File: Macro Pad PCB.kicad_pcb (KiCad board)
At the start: 2 copper layers, 77.8 x 173 mm, 169 parts, among them J1 Debug, Q1 DMG1012T, SW1 PEC11R-4015F-S0024, SW2 PEC11R-4015F-S0024, U1 RP2040, U2 W25Q16JVSNIQ, U3 MIC5365-3.3YC5-TR, U4 IP4234CZ6, Y2 12 MHz

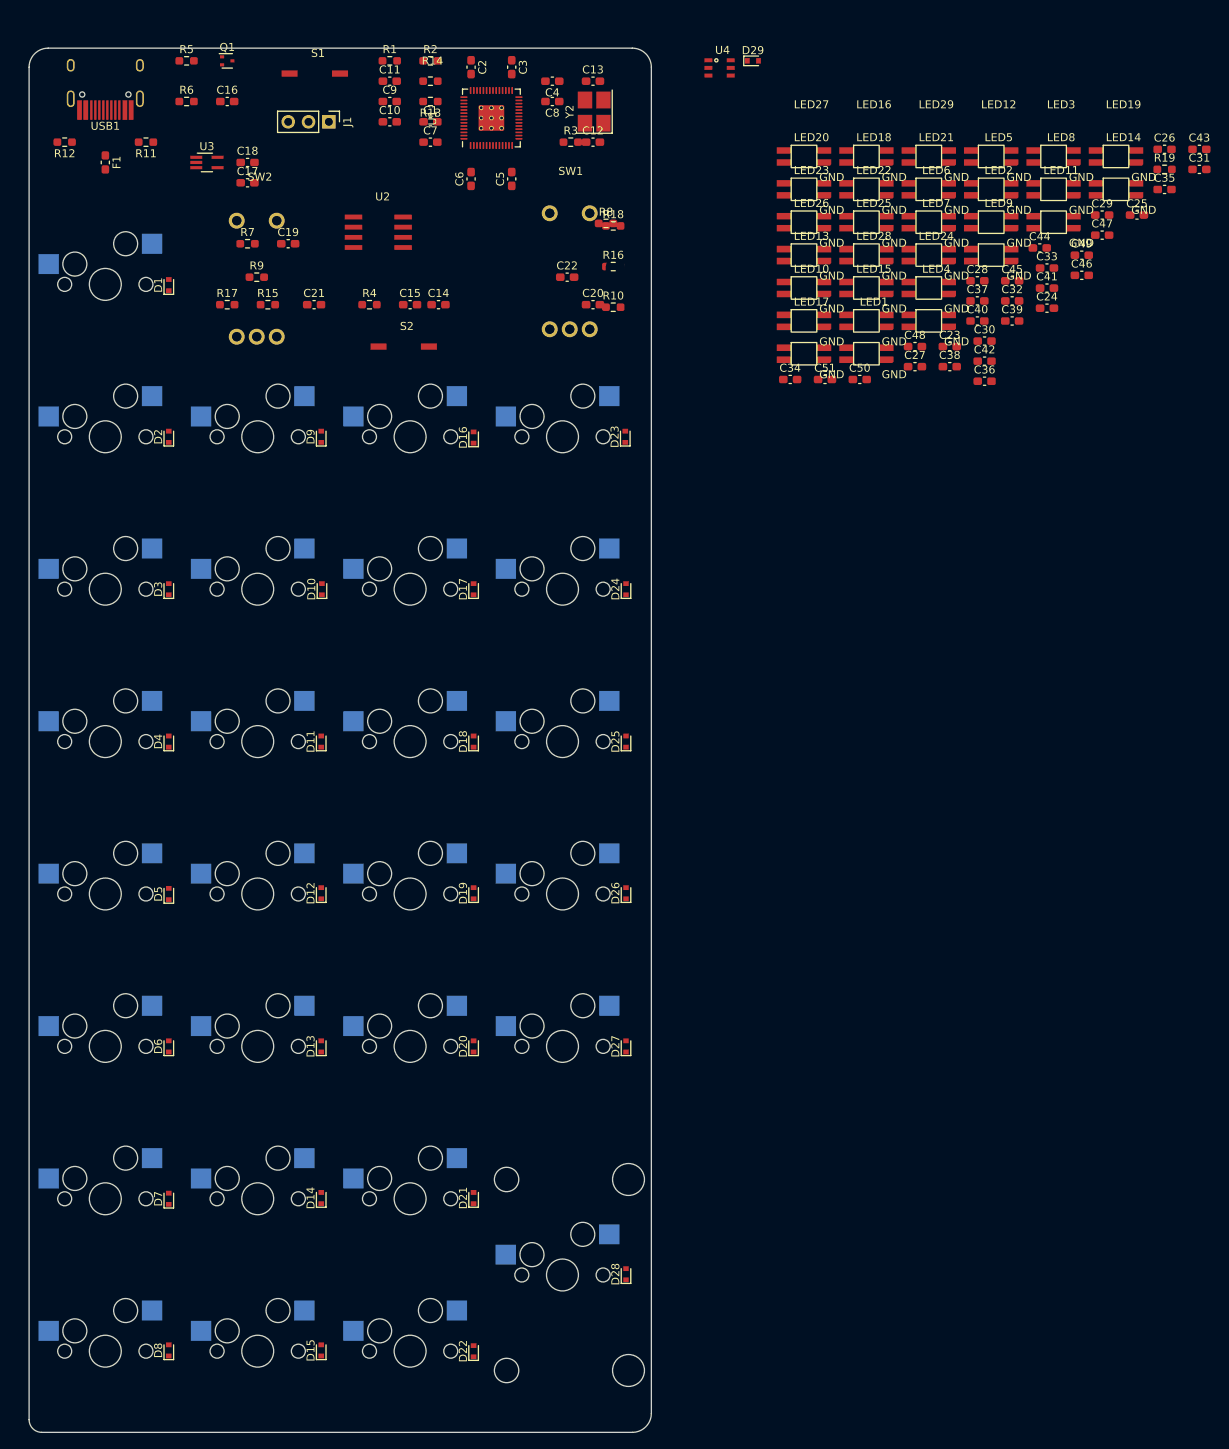
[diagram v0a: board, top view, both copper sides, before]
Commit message: Layout Roughed in, routing started
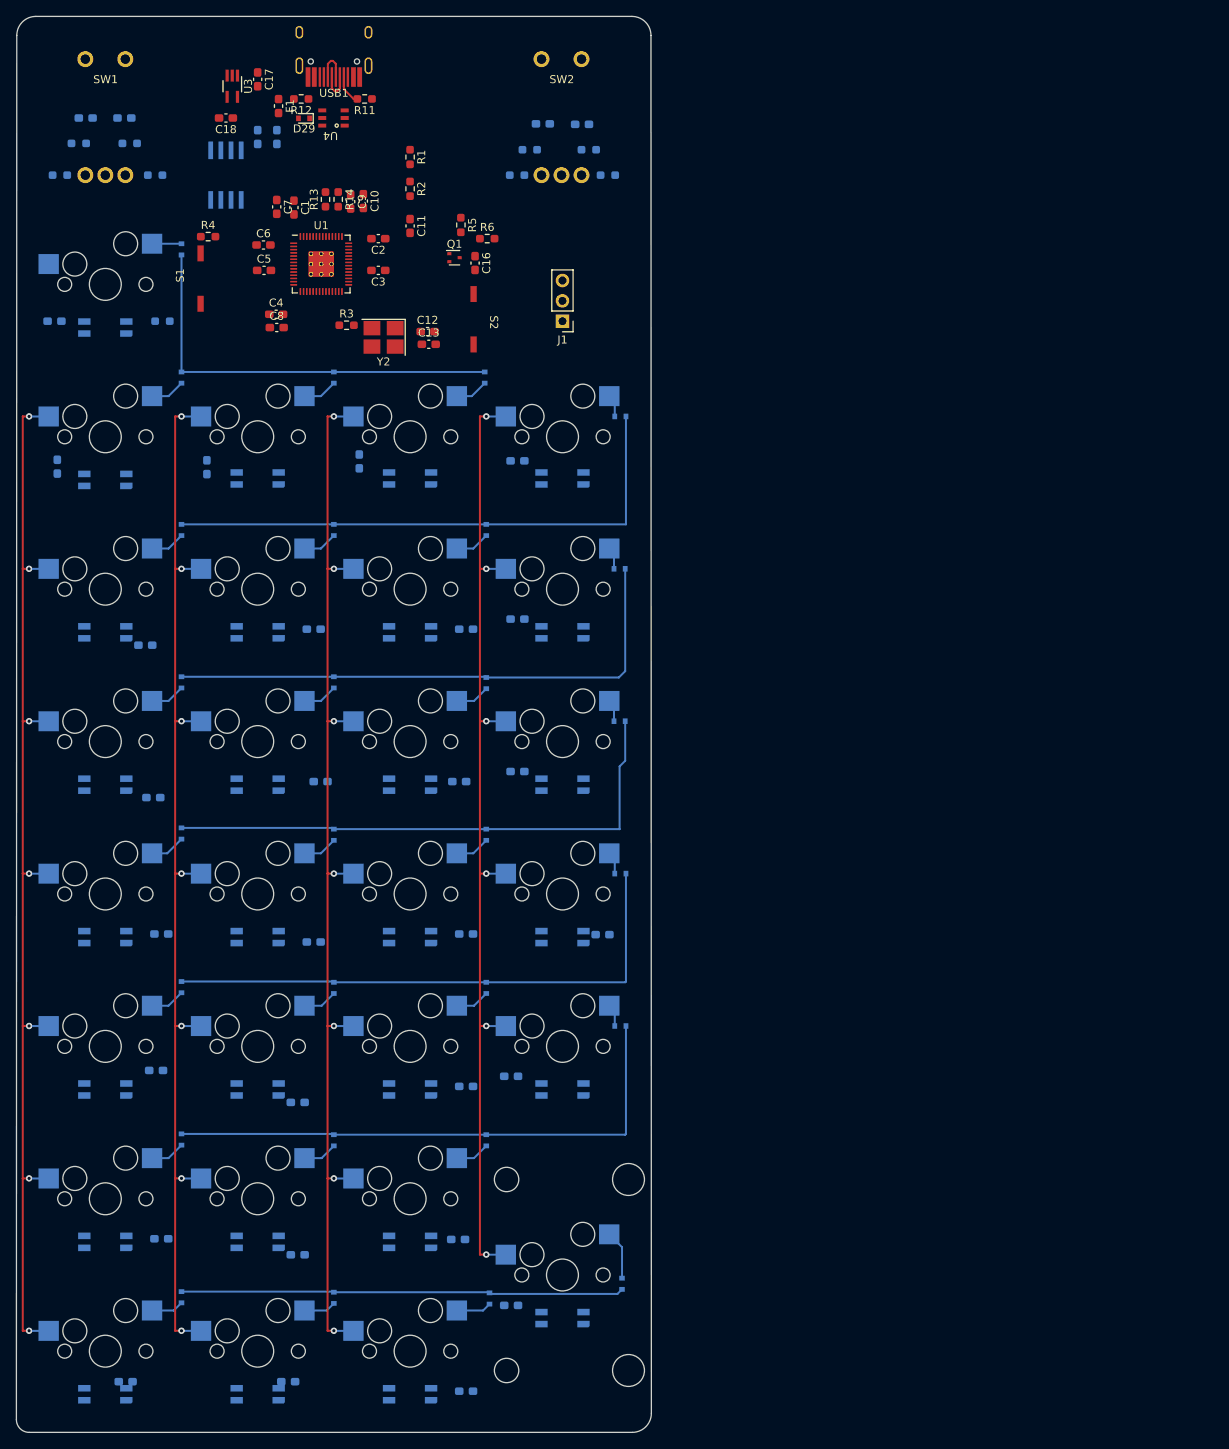
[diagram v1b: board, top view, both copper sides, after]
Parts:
- removed C51: 100nF, Capacitor_SMD:C_0603_1608Metric_Pad1.08x0.95mm_HandSolder
- removed LED29: SK812_Mini-E, Reset Switch:SK812 Mini-E
- C14, C15, C19, C20, C21, C22, C23, C24, C25, C26, C27, C28, C29, C30, C31, C32, C33, C34, C35, C36, C37, C38, C39, C40, C41, C42, C43, C44, C45, C46, C47, C48, C49, C50, D1, D10, D11, D12, D13, D14, D15, D16, D17, D18, D19, D2, D20, D21, D22, D23, D24, D25, D26, D27, D28, D3, D4, D5, D6, D7, D8, D9, R10, R15, R16, R17, R18, R19, R7, R8, R9, U2: moved to B.Cu
- moved LED8 191.7 mm to (49.2, 190.7)
- moved C43 191.6 mm to (73.7, 190.5), turned to 180 degrees
- moved C26 185.1 mm to (57.8, 172.6), turned to 180 degrees
- moved C39 172.8 mm to (53.3, 190.5), turned to 180 degrees
- moved LED14 169.8 mm to (68.2, 171.6)
- moved C47 164.9 mm to (95.9, 191.7), turned to 180 degrees
- moved C29 164.3 mm to (74.8, 174.6), turned to 180 degrees
- moved C35 161.6 mm to (101.5, 181.0), turned to 180 degrees
- moved LED7 160.7 mm to (49.2, 171.6)
- moved LED22 157.2 mm to (87.3, 190.7)
- moved LED15 154.2 mm to (68.2, 190.7)
- moved C25 151.5 mm to (57.8, 134.5), turned to 180 degrees
- moved LED6 149.5 mm to (49.2, 152.6)
- moved LED21 146.7 mm to (87.3, 171.6)
- moved LED5 144.9 mm to (49.2, 133.5)
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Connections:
- D23 pad 1: Row 2 -> Net-(MX23-Pad2)
- D23 pad 2: Net-(D23-Pad2) -> Row 2
- LED22 pad 2: Net-(LED22-Pad2) -> unconnected-(LED22-Pad2)
- MX23 pad 2: Net-(D23-Pad2) -> Net-(MX23-Pad2)
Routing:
- net Col 3: track 0.00 -> 137.0 mm, vias 0 -> 7
- net Col 2: track 0.00 -> 137.0 mm, vias 0 -> 7
- net Col 1: track 0.00 -> 137.0 mm, vias 0 -> 7
- net Col 4: track 0.00 -> 124.2 mm, vias 0 -> 6
- net Row 6: track 0.00 -> 69.1 mm
- net Row 5: track 0.00 -> 69.1 mm
- net Row 2: track 0.00 -> 69.1 mm
- net Row 3: track 0.00 -> 68.6 mm
- net Row 4: track 0.00 -> 68.6 mm
- net Row 7: track 0.00 -> 55.4 mm
- net Row 1: track 0.00 -> 52.8 mm
- net Net-(D28-Pad2): track 0.00 -> 6.14 mm
- net Net-(D3-Pad2): track 0.00 -> 4.92 mm
- net Net-(D16-Pad2): track 0.00 -> 4.72 mm
- net Net-(U4-Pad4): track 0.00 -> 4.61 mm
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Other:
- board size 77.8 x 173 mm -> 79.4 x 177 mm

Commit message: Routing Continued
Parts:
- moved C8 14.8 mm to (86.7, 56.0), turned to 180 degrees
- moved C4 14.5 mm to (86.7, 57.5), turned to 180 degrees
- moved C47 13.3 mm to (82.7, 190.1)
- moved C43 9.51 mm to (64.2, 190.0)
- moved Q1 6.00 mm to (88.6, 48.7), turned to -90 degrees
- moved R6 5.78 mm to (93.4, 50.2), turned to -90 degrees
- moved F1 5.48 mm to (72.9, 25.6)
- moved C16 5.24 mm to (91.8, 50.2)
- moved C23 4.96 mm to (49.0, 56.0), turned to 0 degrees
- moved C7 4.77 mm to (75.2, 40.0)
- moved C13 4.60 mm to (86.7, 61.4)
- moved C1 4.48 mm to (76.8, 40.0)
- moved C12 4.41 mm to (86.7, 59.1)
- moved Y2 4.40 mm to (81.2, 60.3)
- moved C9 3.06 mm to (81.8, 40.0)
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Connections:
- net Net-(R13-Pad2) renamed d2P
- net Net-(R14-Pad2) renamed d2N
- net Net-(U4-Pad3) renamed dN
- net Net-(U4-Pad4) renamed dP
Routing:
- net Earth: track 0.00 -> 300.6 mm, vias 0 -> 5
- net +5V: track 0.00 -> 116.8 mm, vias 0 -> 3
- net +3.3V: track 0.00 -> 77.8 mm, vias 0 -> 4
- net ENC2 B: track 0.00 -> 57.2 mm, vias 0 -> 1
- net ENC SW2: track 0.00 -> 47.5 mm, vias 0 -> 1
- net VCC: track 0.00 -> 45.2 mm, vias 0 -> 5
- net ENC2 A: track 0.00 -> 42.3 mm, vias 0 -> 1
- net LED DIN: track 0.00 -> 33.5 mm, vias 0 -> 3
- net SWCLK: track 0.00 -> 32.6 mm, vias 0 -> 1
- net SWDIO: track 0.00 -> 31.5 mm, vias 0 -> 1
- net +1V1: track 0.00 -> 27.0 mm, vias 0 -> 2
- net QSPI_SD0: track 0.00 -> 23.6 mm, vias 0 -> 1
- net QSPI_SCLK: track 0.00 -> 22.9 mm, vias 0 -> 1
- net QSPI_SD3: track 0.00 -> 21.8 mm, vias 0 -> 1
- net Xin: track 0.00 -> 18.6 mm
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
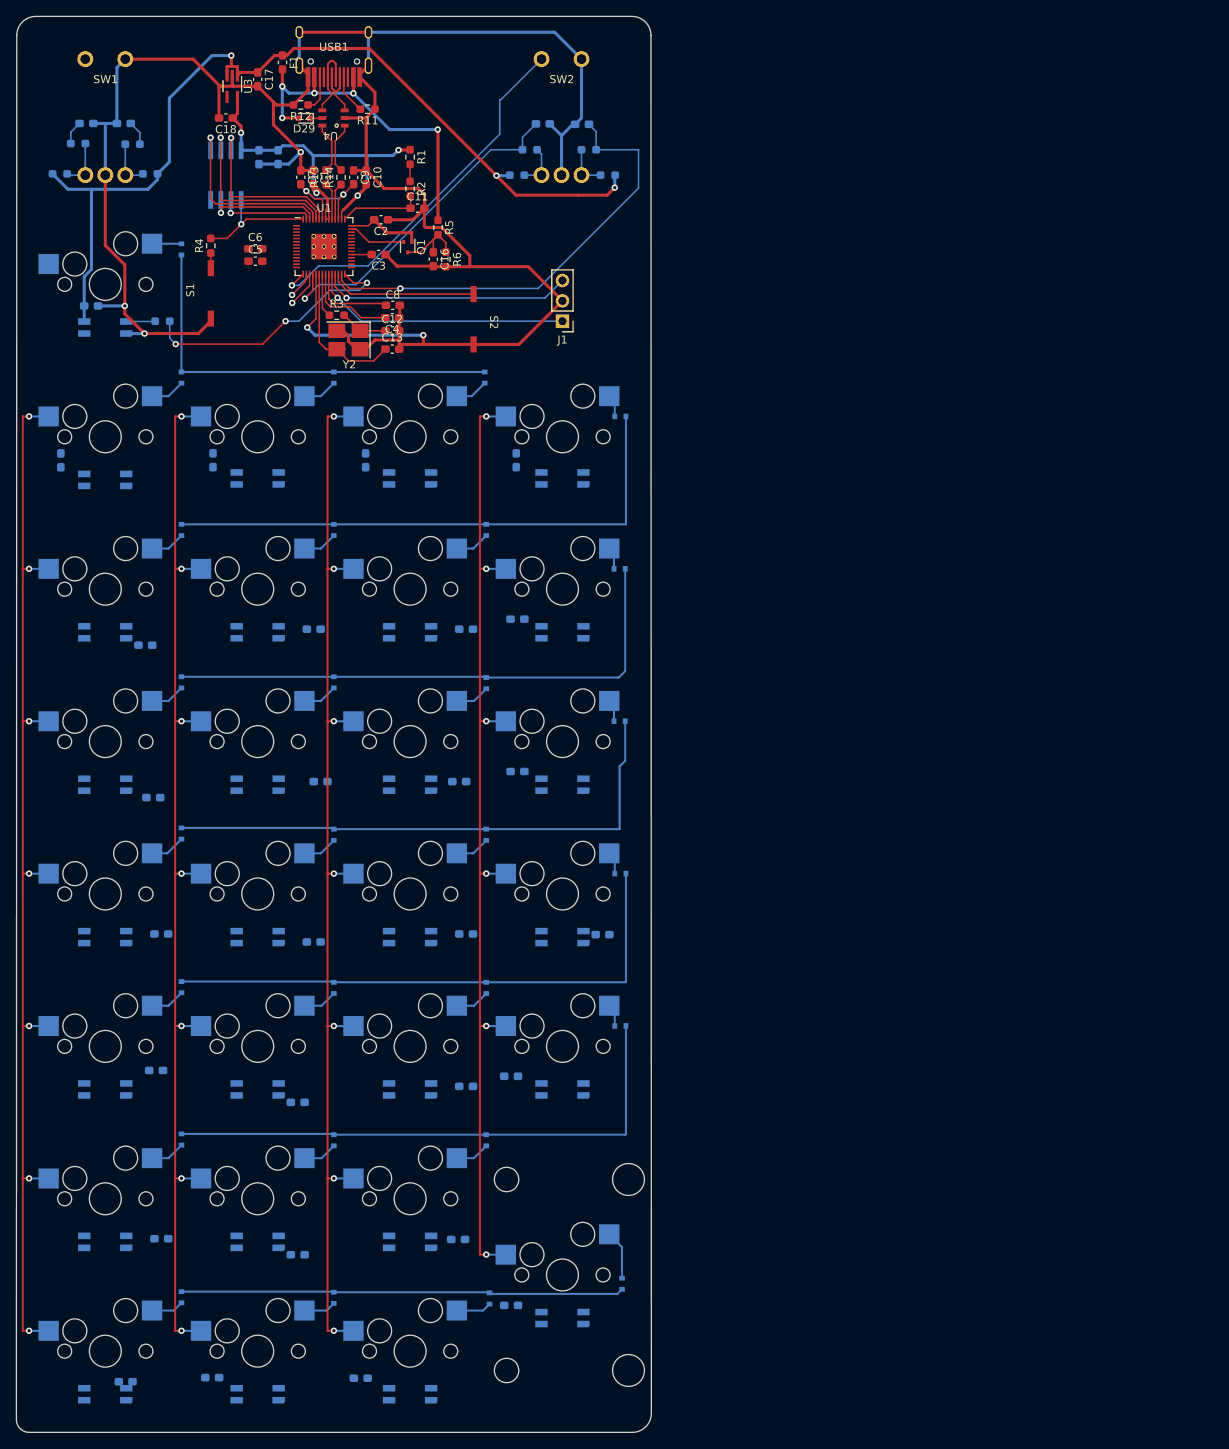
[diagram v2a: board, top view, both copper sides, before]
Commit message: Routing Finished and ESD Protection Enhanced
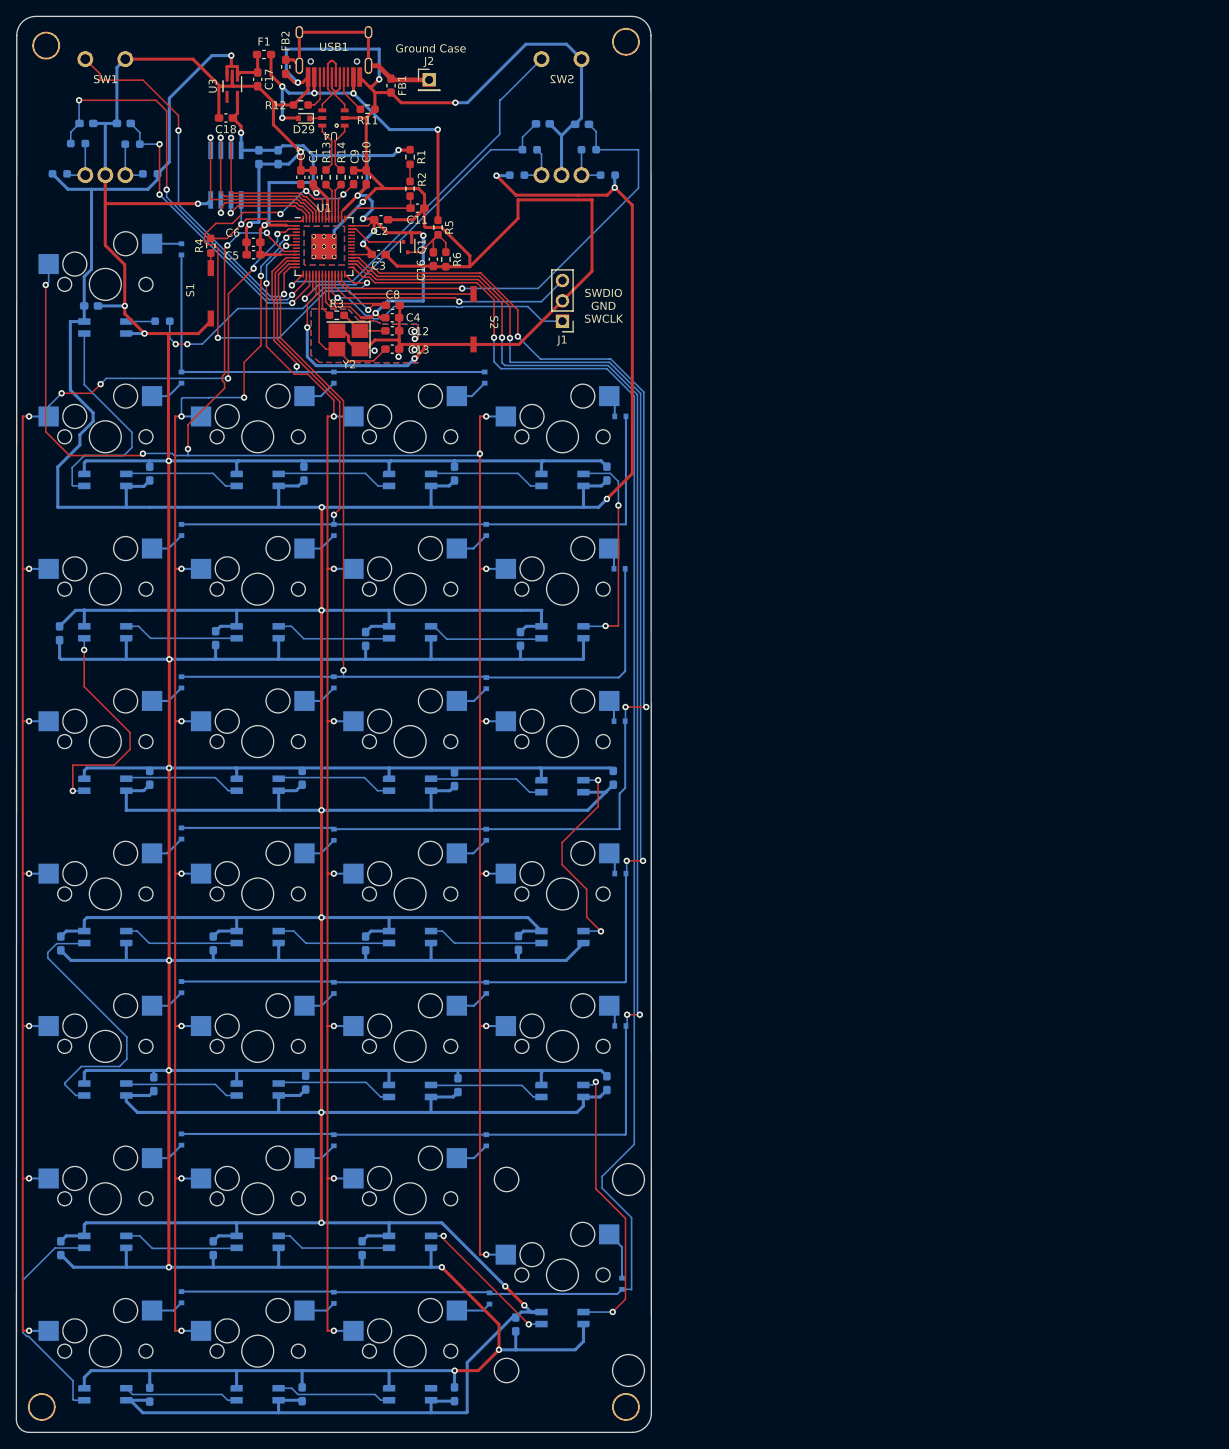
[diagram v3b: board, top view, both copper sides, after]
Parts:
- added FB1: 70@100MHz, Inductor_SMD:L_0603_1608Metric_Pad1.05x0.95mm_HandSolder, F.Cu at (86.5, 28.5)
- added FB2: 70@100MHz, Inductor_SMD:L_0603_1608Metric_Pad1.05x0.95mm_HandSolder, F.Cu at (73.4, 26.2)
- added H1: 3mm_Hole, Reset Switch:3mm Hole, F.Cu at (43.4, 23.5)
- added H2: 3mm_Hole, Reset Switch:3mm Hole, F.Cu at (115.9, 23.0)
- added H3: 3mm_Hole, Reset Switch:3mm Hole, F.Cu at (42.9, 193.7)
- added H4: 3mm_Hole, Reset Switch:3mm Hole, F.Cu at (115.9, 193.7)
- added J2: SHIELD CON, Connector_PinHeader_2.54mm:PinHeader_1x01_P2.54mm_Vertical, F.Cu at (91.3, 27.8)
- moved C30 12.6 mm to (83.3, 97.7), turned to -90 degrees
- moved C31 12.6 mm to (83.3, 135.7), turned to -90 degrees
- moved C25 12.6 mm to (45.2, 135.7), turned to -90 degrees
- moved C26 12.6 mm to (45.2, 173.8), turned to -90 degrees
- moved C28 12.6 mm to (64.3, 135.7), turned to -90 degrees
- moved C27 12.3 mm to (64.6, 97.6), turned to -90 degrees
- moved C32 12.1 mm to (82.9, 173.8), turned to -90 degrees
- moved C50 12.0 mm to (113.5, 153.2), turned to 90 degrees
- moved C49 12.0 mm to (114.3, 115.0), turned to 90 degrees
- moved C47 11.9 mm to (94.5, 192.1), turned to 90 degrees
- moved C40 11.5 mm to (75.6, 77.0)
- moved C48 11.5 mm to (113.5, 77.0)
- moved C43 11.4 mm to (75.4, 192.1), turned to 90 degrees
- moved C44 11.2 mm to (94.5, 77.0)
- moved C36 11.2 mm to (56.4, 77.0)
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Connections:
- U1 pad 11: Row 5 -> Row 1
- U1 pad 12: Row 6 -> Row 2
- U1 pad 13: Row 7 -> Row 3
- U1 pad 29: unconnected-(U1-Pad29) -> Row 7
- U1 pad 3: Col 2 -> unconnected-(U1-Pad3)
- U1 pad 30: unconnected-(U1-Pad30) -> Row 6
- U1 pad 31: unconnected-(U1-Pad31) -> Row 5
- U1 pad 32: unconnected-(U1-Pad32) -> Row 4
- U1 pad 4: Col 3 -> Col 2
- U1 pad 5: Col 4 -> unconnected-(U1-Pad5)
- U1 pad 6: Row 1 -> unconnected-(U1-Pad6)
- U1 pad 7: Row 2 -> Col 3
- U1 pad 8: Row 3 -> unconnected-(U1-Pad8)
- U1 pad 9: Row 4 -> Col 4
- USB1 pad 13: Earth -> Net-(FB1-Pad1)
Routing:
- net Earth: track 300.6 -> 1019.1 mm, vias 5 -> 25
- net +5V: track 116.8 -> 797.4 mm, vias 3 -> 12
- net Row 7: track 55.4 -> 218.1 mm, vias 0 -> 1
- net Row 6: track 69.1 -> 196.7 mm, vias 0 -> 3
- net Col 4: track 124.2 -> 240.0 mm, vias 6 -> 12
- net Row 5: track 69.1 -> 178.4 mm, vias 0 -> 3
- net Row 4: track 68.6 -> 157.9 mm, vias 0 -> 3
- net Row 3: track 68.6 -> 125.1 mm, vias 0 -> 1
- net +1V1: track 27.0 -> 80.9 mm, vias 2 -> 5
- net +3.3V: track 77.8 -> 129.8 mm, vias 4 -> 10
- net ENC SW1: track 0.00 -> 48.7 mm, vias 0 -> 2
- net Col 1: track 137.0 -> 185.4 mm, vias 7 -> 12
- net ENC1 A: track 6.32 -> 52.7 mm, vias 1 -> 3
- net Row 2: track 69.1 -> 107.4 mm, vias 0 -> 1
- net Net-(LED27-Pad2): track 0.00 -> 36.3 mm, vias 0 -> 2
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- added copper zone on B.Cu, net Earth
- added copper zone on F.Cu, net Earth
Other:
- board text added: "Ground Case"
- board text added: "NumM Pad V1.0 Designed by Jacob OBrien"
- board text added: "SWDIO GND SWCLK"
